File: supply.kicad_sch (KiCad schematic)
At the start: 57 parts, among them U1 AP7330-W5-7, U2 AP7330-W5-7, U3 AP7330-W5-7, U4 AP62301WU-7, U5 AP62301WU-7, U6 AP62301WU-7

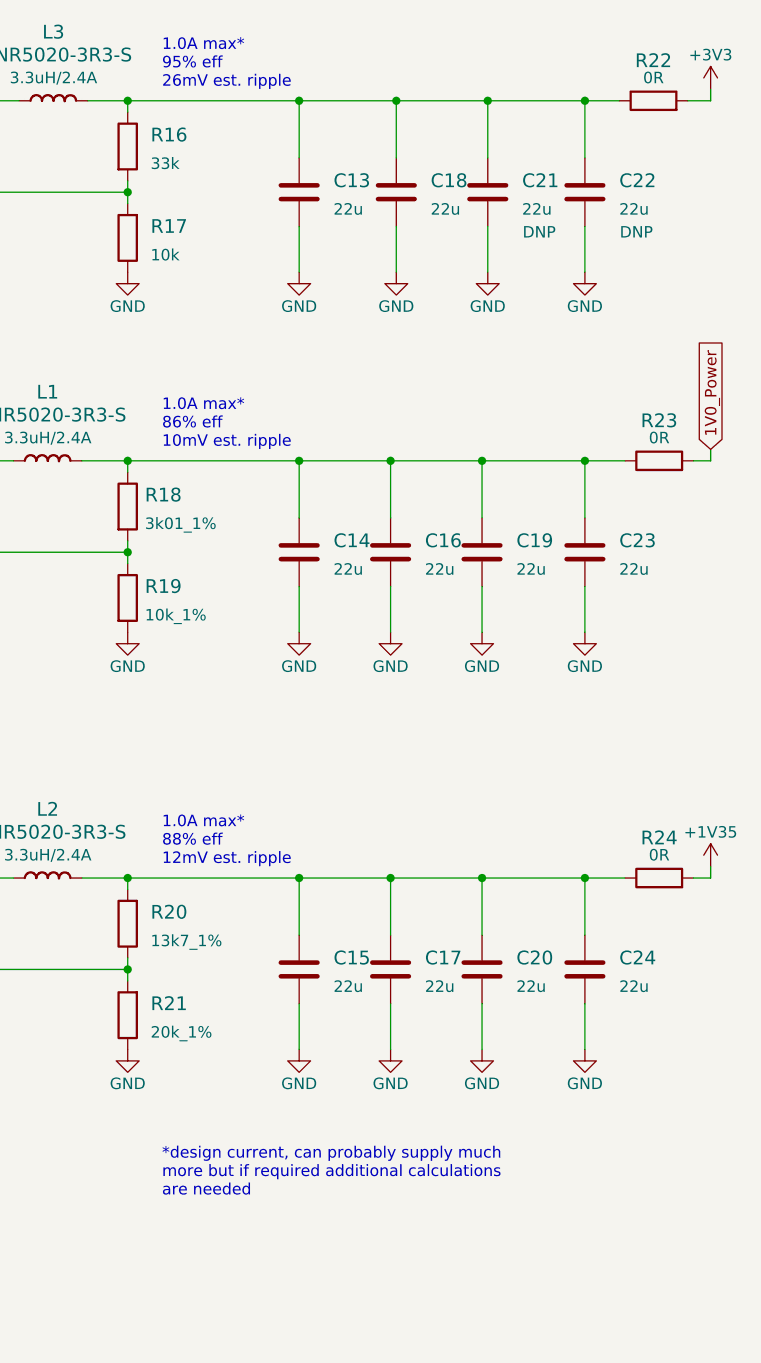
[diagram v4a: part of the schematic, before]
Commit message: Recalculated PSU SMPSs ratings
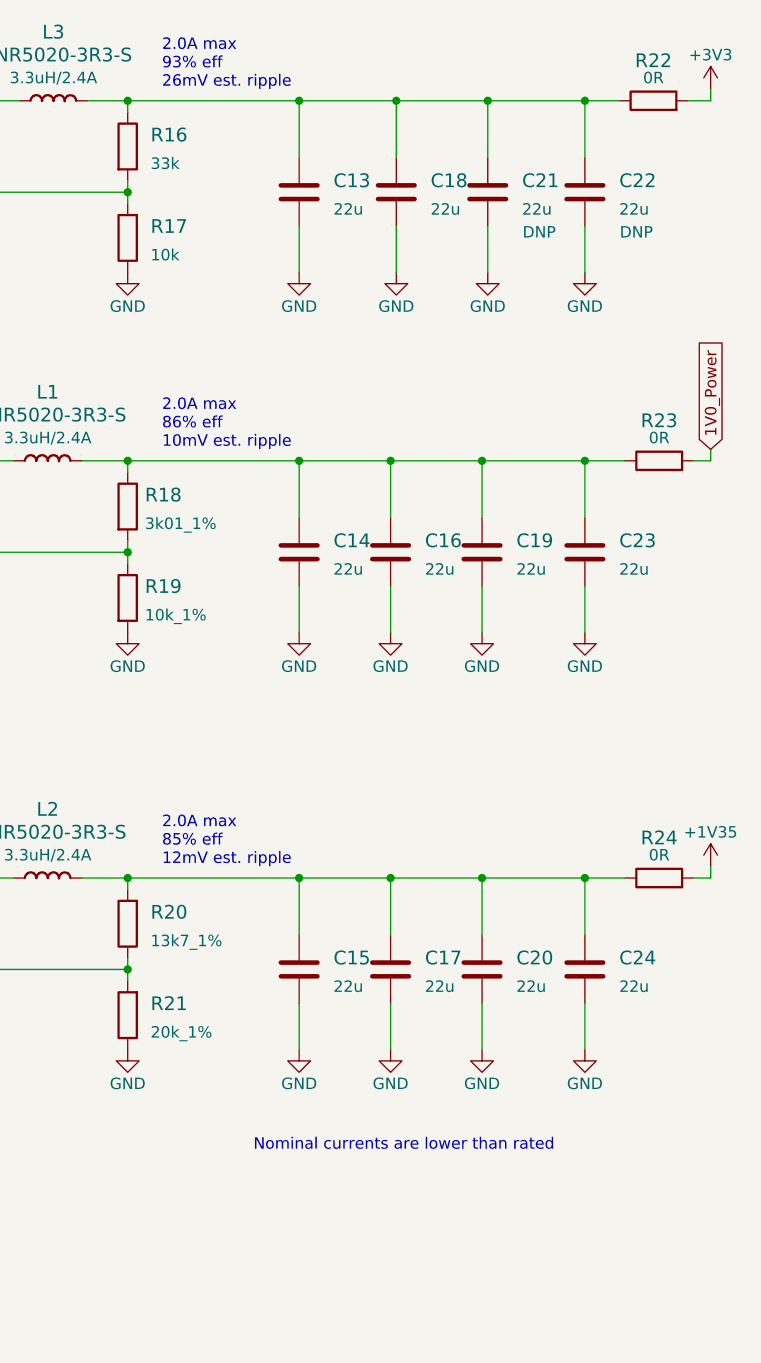
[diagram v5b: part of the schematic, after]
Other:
- note added: "2.0A max 85% eff 12mV est. ripple"
- note added: "2.0A max 86% eff 10mV est. ripple"
- note added: "2.0A max 93% eff 26mV est. ripple"
- note added: "Nominal currents are lower than rated"
- note removed: "*design current, can probably supply much more but if required additional calculations are needed"
- note removed: "1.0A max* 86% eff 10mV est. ripple"
- note removed: "1.0A max* 88% eff 12mV est. ripple"
- note removed: "1.0A max* 95% eff 26mV est. ripple"
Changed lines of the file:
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@@
     (stroke (width 0) (type default) (color 0 0 0 0))
   )
-  (text "*design current, can probably supply much\nmore but if required additional calculations\nare needed"
-    (at 207.01 149.86 0)
+  (text "Nominal currents are lower than rated" (at 217.17 144.78 0)
     (effects (font (size 1.27 1.27)) (justify left bottom))
   )
-  (text "1.0A max*\n95% eff\n26mV est. ripple\n" (at 207.01 26.67 0)
+  (text "2.0A max\n93% eff\n26mV est. ripple\n" (at 207.01 26.67 0)
     (effects (font (size 1.27 1.27)) (justify left bottom))
   )
-  (text "1.0A max*\n88% eff\n12mV est. ripple\n" (at 207.01 113.03 0)
+  (text "2.0A max\n85% eff\n12mV est. ripple\n" (at 207.01 113.03 0)
     (effects (font (size 1.27 1.27)) (justify left bottom))
   )
-  (text "1.0A max*\n86% eff\n10mV est. ripple\n" (at 207.01 66.675 0)
+  (text "2.0A max\n86% eff\n10mV est. ripple\n" (at 207.01 66.675 0)
     (effects (font (size 1.27 1.27)) (justify left bottom))
   )

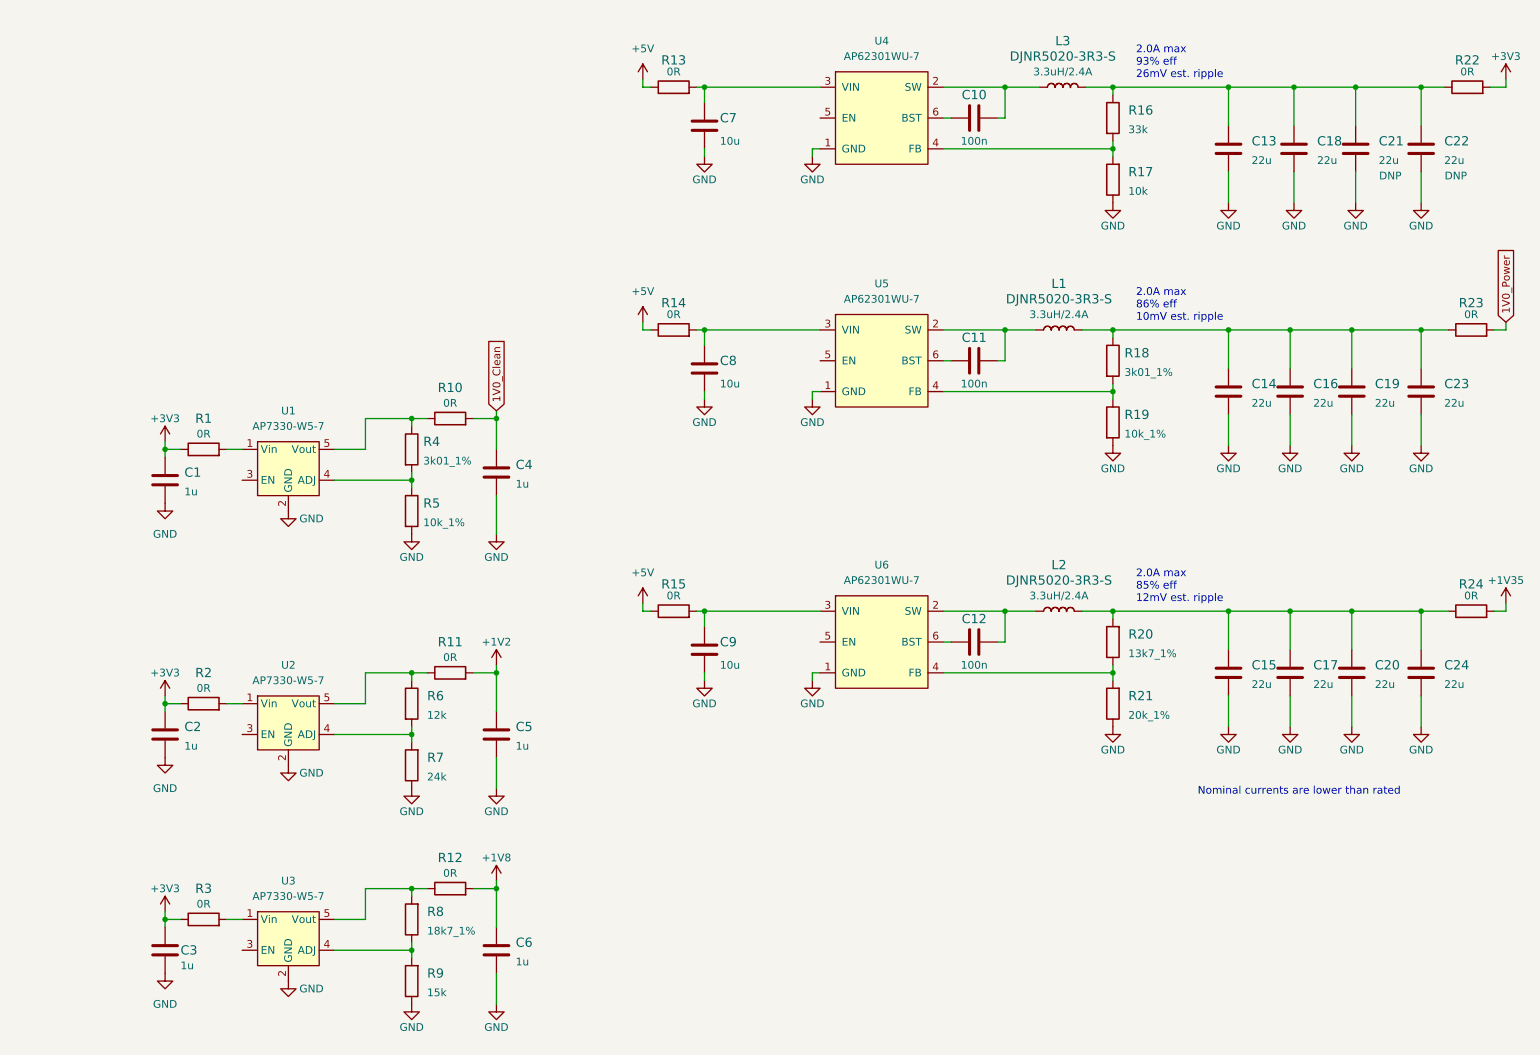
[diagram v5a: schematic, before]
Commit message: Added DDR3 Vtt and Vref regulator
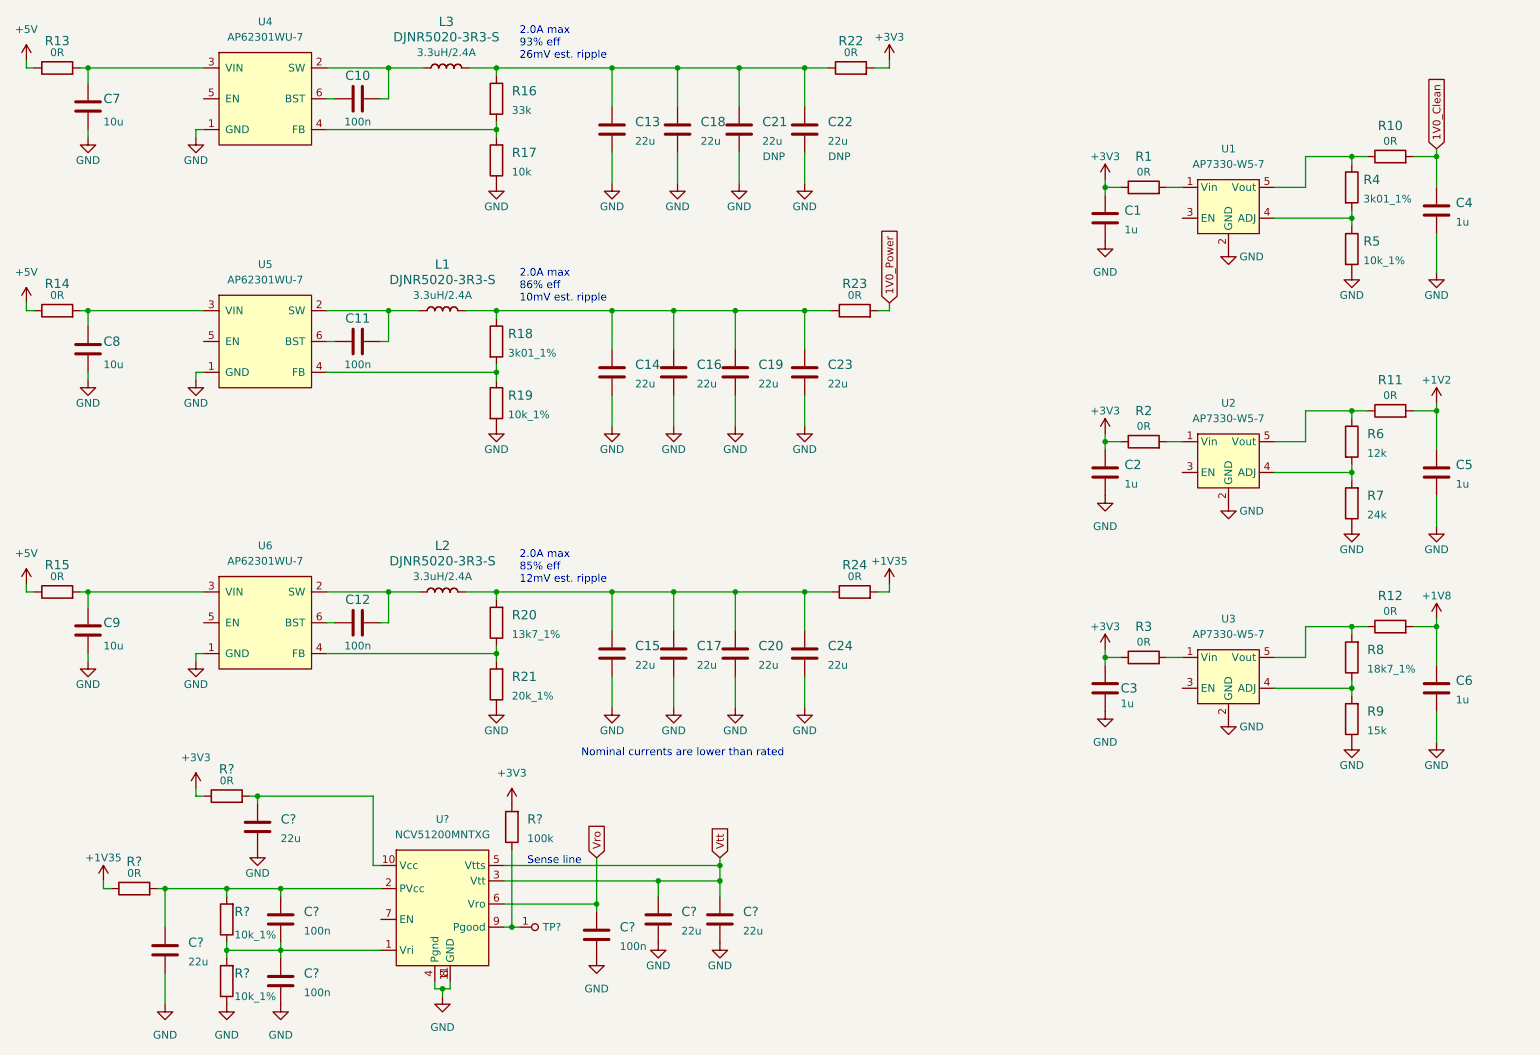
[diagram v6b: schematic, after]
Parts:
- added C? (x3): C_100n_0402, antmicro-footprints:0402-cap, symbol antmicroCapacitors0402:C_100n_0402
- added C? (x4): C_22u_0805, antmicro-footprints:0805-cap, symbol antmicroCapacitorsmisc:C_22u_0805
- added R? (x2): R_10k_1%_0603, antmicro-footprints:0603-res, symbol antmicroResistors0603:R_10k_1%_0603
- added R? (x2): R_0R_0805, antmicro-footprints:0805-res, symbol antmicroResistorsmisc:R_0R_0805
- added R?: R_100k_0603, antmicro-footprints:0603-res, symbol antmicroResistors0603:R_100k_0603
- added TP?: TP, antmicro-footprints:TP-R-1.5, symbol antmicroTestPoints:TP
- added U?: NCV51200MNTXG, antmicro-footprints:DFN-10-1EP_3x3mm, symbol antmicroPMICVoltageRegulatorsLinear:NCV51200MNTXG
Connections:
- net +1V35: now also R?.1
- net +3V3: now also R?.1, R?.2
- net GND: now also C?.2, C?.2, C?.2, C?.2, C?.2, C?.2, R?.1, U?.11 (GND), U?.4 (Pgnd), U?.8 (GND)
- new net: C?.1, C?.2, R?.1, R?.2, U?.1 (Vri)
- new net: C?.1, R?.2, U?.10 (Vcc)
- new net: C?.1, C?.1, R?.2, R?.2, U?.2 (PVcc)
- new net: R?.1, TP?.1, U?.9 (Pgood)
- new net Vro: C?.1, U?.6 (Vro)
- new net Vtt: C?.1, C?.1, U?.3 (Vtt), U?.5 (Vtts)
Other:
- note added: "Sense line"
- moved on the sheet: C1, C10, C11, C12, C13, C14, C15, C16, C17, C18, C19, C2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

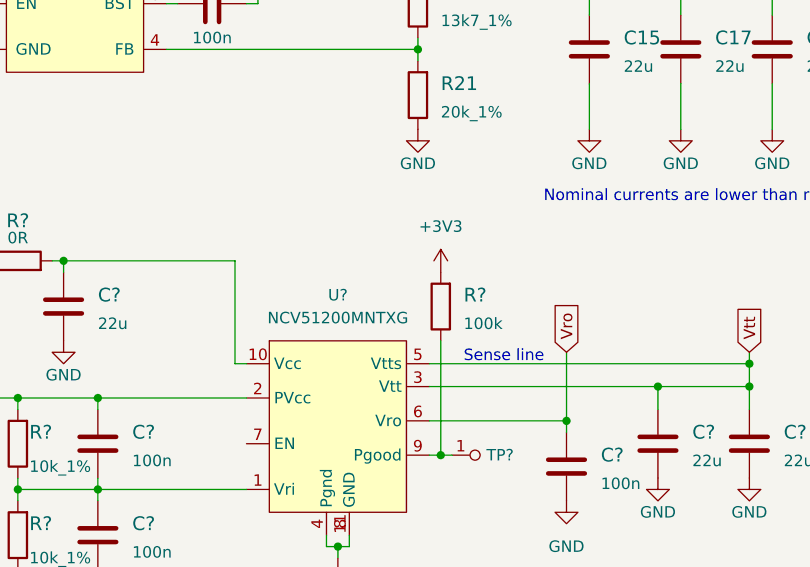
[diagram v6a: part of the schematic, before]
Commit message: Fixed VREF connection
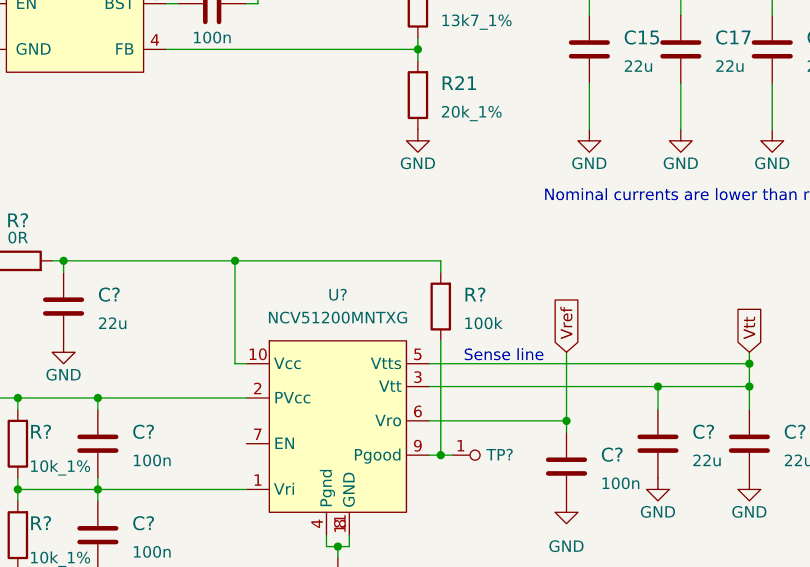
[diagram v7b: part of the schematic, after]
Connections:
- net +3V3: no longer R?.2
- net at C?.1, R?.2, U?.10 (Vcc): now also R?.2
- net Vro renamed Vref
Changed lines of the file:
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@@
   (junction (at 104.14 166.37) (diameter 0) (color 0 0 0 0)
   )
+  (junction (at 81.28 144.78) (diameter 0) (color 0 0 0 0)
+  )
   (junction (at 130.81 111.125) (diameter 0) (color 0 0 0 0)
   )
@@
     (stroke (width 0) (type default) (color 0 0 0 0))
   )
+  (wire (pts (xy 81.28 144.78) (xy 104.14 144.78))
+    (stroke (width 0) (type default) (color 0 0 0 0))
+  )
   (wire (pts (xy 229.87 91.44) (xy 242.57 91.44))
     (stroke (width 0) (type default) (color 0 0 0 0))
@@
   )
   (wire (pts (xy 131.445 38.735) (xy 131.445 43.815))
+    (stroke (width 0) (type default) (color 0 0 0 0))
+  )
+  (wire (pts (xy 104.14 144.78) (xy 104.14 146.05))
     (stroke (width 0) (type default) (color 0 0 0 0))
   )
@@
   (text "2.0A max\n86% eff\n10mV est. ripple\n" (at 105.41 63.5 0)
     (effects (font (size 1.27 1.27)) (justify left bottom))
+  )
+  (global_label "Vref" (shape input) (at 118.11 154.94 90) (fields_autoplaced)
+    (effects (font (size 1.27 1.27)) (justify left))
+    (property "Intersheet References" "${INTERSHEET_REFS}" (id 0) (at 118.0306 148.8379 90)
+      (effects (font (size 1.27 1.27)) (justify left) hide)
+    )
   )
   (global_label "1V0_Clean" (shape input) (at 256.54 38.1 90) (fields_autoplaced)
@@
     (effects (font (size 1.27 1.27)) (justify left))
     (property "Intersheet References" "${INTERSHEET_REFS}" (id 0) (at 138.3506 149.9869 90)
-      (effects (font (size 1.27 1.27)) (justify left) hide)
-    )
-  )
-  (global_label "Vro" (shape input) (at 118.11 154.94 90) (fields_autoplaced)
-    (effects (font (size 1.27 1.27)) (justify left))
-    (property "Intersheet References" "${INTERSHEET_REFS}" (id 0) (at 118.0306 149.5031 90)
       (effects (font (size 1.27 1.27)) (justify left) hide)
     )
@@
     (pin "2")
   )
-  (symbol (lib_id "power:+3V3") (at 104.14 146.05 0) (unit 1)
-    (in_bom yes) (on_board yes) (fields_autoplaced)
-    (property "Reference" "#PWR?" (id 0) (at 104.14 149.86 0)
-      (effects (font (size 1.27 1.27)) hide)
-    )
-    (property "Value" "+3V3" (id 1) (at 104.14 140.97 0))
-    (property "Footprint" "" (id 2) (at 104.14 146.05 0)
-      (effects (font (size 1.27 1.27)) hide)
-    )
-    (property "Datasheet" "" (id 3) (at 104.14 146.05 0)
-      (effects (font (size 1.27 1.27)) hide)
-    )
-    (pin "1")
-  )
   (symbol (lib_id "antmicroResistors0603:R_13k7_1%_0603") (at 101.6 116.205 90) (unit 1)
